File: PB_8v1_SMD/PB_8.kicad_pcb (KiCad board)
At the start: 2 copper layers, 86.4 x 100.2 mm, 62 parts, among them J1 String1, J18 Power In Right, J19 USB, J2 String2, J23 VIN Voltage, J25 RTC Conn, J26 OLED Conn, J27 GPIO Header, J28 Aux Pwr, J29 VIN Select, J3 String3, J4 String4, J5 String5, J6 String6, J7 String7, J8 String8, Q1 DMP3056L, SW1 Enter BTN, SW2 Down BTN, SW3 OLED Select, U1 OKI-78SR-5, U2 24LC256, U3 POCKETBEAGLE-SC-569, U5 SN74HCT245N, U8 TPS2051BDBVR, U9 TPD4S009DBVR

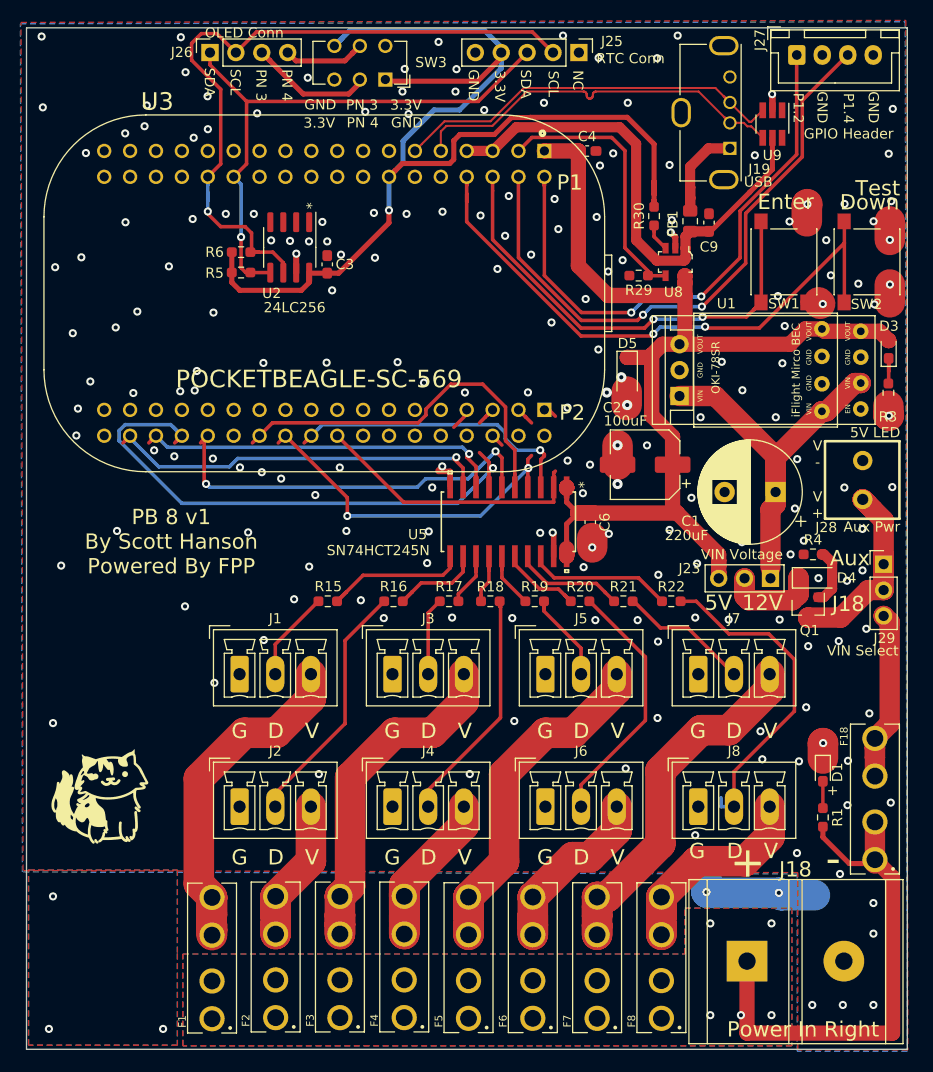
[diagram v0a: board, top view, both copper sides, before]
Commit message: Add Diff out 9-12
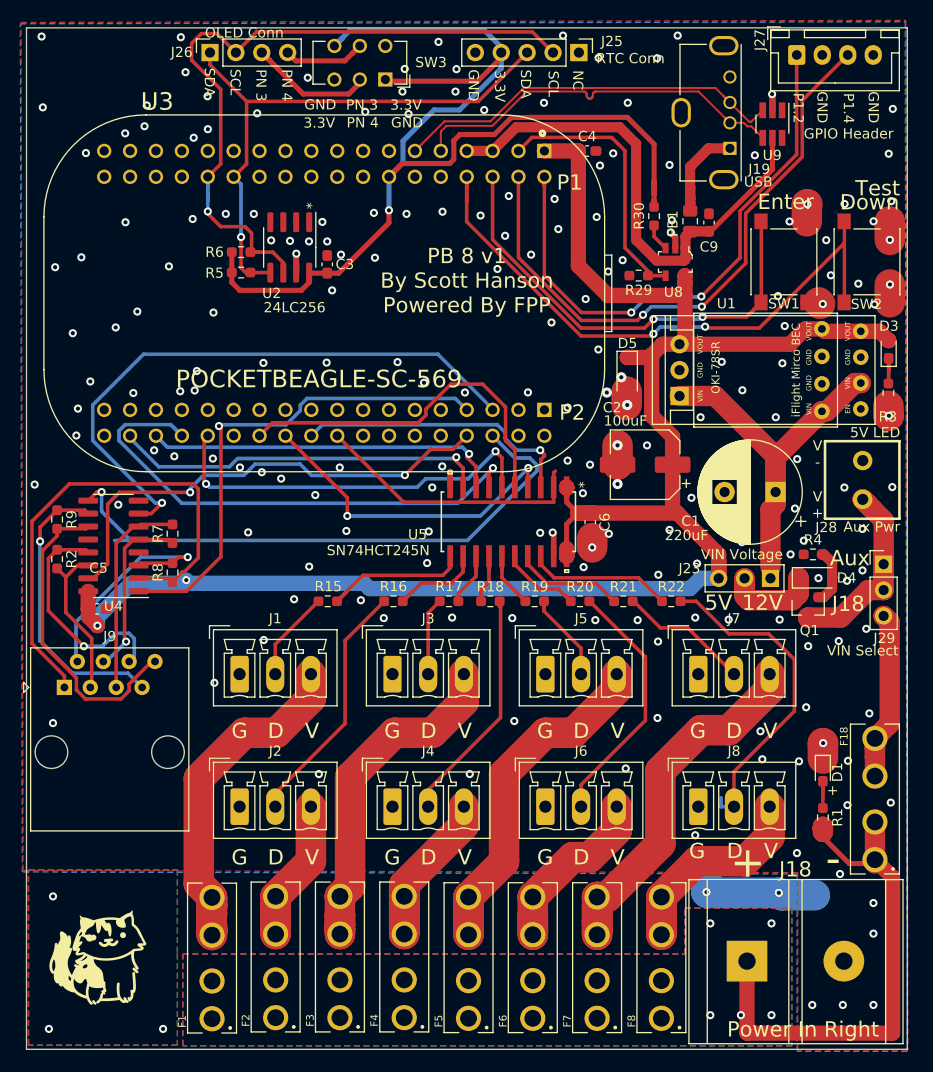
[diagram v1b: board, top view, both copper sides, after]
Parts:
- added C5: 0.1uF, Capacitor_SMD:C_0603_1608Metric_Pad1.08x0.95mm_HandSolder, F.Cu at (135.1, 110.2)
- added J9: RJ45, Connector_RJ:RJ45_Amphenol_54602-x08_Horizontal, F.Cu at (131.9, 117.9)
- added R2: 120, Resistor_SMD:R_0603_1608Metric_Pad0.98x0.95mm_HandSolder, F.Cu at (131.2, 105.3)
- added R7: 120, Resistor_SMD:R_0603_1608Metric_Pad0.98x0.95mm_HandSolder, F.Cu at (142.5, 102.8)
- added R8: 120, Resistor_SMD:R_0603_1608Metric_Pad0.98x0.95mm_HandSolder, F.Cu at (142.5, 106.6)
- added R9: 120, Resistor_SMD:R_0603_1608Metric_Pad0.98x0.95mm_HandSolder, F.Cu at (131.2, 101.4)
- added U4: AM26C31, Package_SO:SOIC-16_3.9x9.9mm_P1.27mm, F.Cu at (136.7, 104.0)
- moved G*** 15.8 mm to (135.0, 143.2)
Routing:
- net +5V: track 107.1 -> 175.0 mm, vias 0 -> 2
- net DATA11: track 2.32 -> 59.9 mm, vias 0 -> 1
- net DATA12: track 2.43 -> 59.1 mm, vias 0 -> 1
- net OUT9+: track 0.00 -> 49.4 mm
- net DATA10: track 0.00 -> 47.5 mm, vias 0 -> 2
- net DATA9: track 2.45 -> 49.2 mm, vias 0 -> 1
- net OUT12-: track 0.00 -> 30.9 mm
- net OUT12+: track 0.00 -> 28.6 mm, vias 0 -> 1
- net OUT9-: track 0.00 -> 22.7 mm, vias 0 -> 1
- net OUT10-: track 0.00 -> 22.6 mm, vias 0 -> 1
- net OUT11+: track 0.00 -> 20.4 mm
- net OUT11-: track 0.00 -> 17.5 mm, vias 0 -> 1
- net OUT10+: track 0.00 -> 15.8 mm
- net DATA3: track 55.5 -> 52.2 mm
- net DATA6: track 36.1 -> 33.4 mm
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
